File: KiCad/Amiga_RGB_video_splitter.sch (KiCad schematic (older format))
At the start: 5 parts, among them J1 DB23_Female-Connector, J2 DB15_Female_HighDensity_Mount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, J3 KMDGX-9S-BS-1, J4 PJ-320A, U1 THS7374IPWR

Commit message: Add capacitor and route VCC to pin 10 on U1, add resistor R1 to Csync line
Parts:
- added C2: 0.1uF, Capacitor_SMD:C_0805_2012Metric_Pad1.18x1.45mm_HandSolder, symbol Device:C_Small
- added R?: R_Small, Resistor_SMD:R_1206_3216Metric_Pad1.30x1.75mm_HandSolder, symbol Device:R_Small
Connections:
- net +5V: now also U1.10 (VS+), C2.1
- net CSYNC: now also R?.1; no longer J3.4
- net GND: now also C2.2
- new net: J3.4, R?.2
- no-connect marks 12 -> 20
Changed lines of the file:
@@
 GND
 NoConn ~ 1650 3700
-Wire Wire Line
-	4300 2700 4300 3900
 $Comp
 L Amiga_RGB_video_splitter:THS7374IPWR U1
@@
 Wire Wire Line
 	3550 5600 3650 5600
+NoConn ~ 2400 4350
+NoConn ~ 3800 4350
+Text GLabel 4150 4150 2    50   Input ~ 0
+VCC
+$Comp
+L Device:C_Small C2
+U 1 1 6832D346
+P 3950 4250
+F 0 "C2" H 4042 4296 50  0000 L CNN
+F 1 "0.1uF" H 4042 4205 50  0000 L CNN
+F 2 "Capacitor_SMD:C_0805_2012Metric_Pad1.18x1.45mm_HandSolder" H 3950 4250 50  0001 C CNN
+F 3 "~" H 3950 4250 50  0001 C CNN
+	1    3950 4250
+	1    0    0    -1
+$EndComp
+Text GLabel 3950 4350 3    50   Input ~ 0
+GND
+Wire Wire Line
+	3800 4150 3950 4150
+Connection ~ 3950 4150
+Wire Wire Line
+	3950 4150 4150 4150
+NoConn ~ 3450 5600
+NoConn ~ 2850 5000
+NoConn ~ 3050 5000
+NoConn ~ 3650 5000
+NoConn ~ 3350 5600
+$Comp
+L Device:R_Small R?
+U 1 1 68333376
+P 4300 3350
+F 0 "R?" H 4359 3396 50  0000 L CNN
+F 1 "R_Small" H 4359 3305 50  0000 L CNN
+F 2 "Resistor_SMD:R_1206_3216Metric_Pad1.30x1.75mm_HandSolder" H 4300 3350 50  0001 C CNN
+F 3 "~" H 4300 3350 50  0001 C CNN
+	1    4300 3350
+	1    0    0    -1
+$EndComp
+NoConn ~ 4400 2700
+Wire Wire Line
+	4300 2700 4300 3250
+Wire Wire Line
+	4300 3900 4300 3450
 $EndSCHEMATC

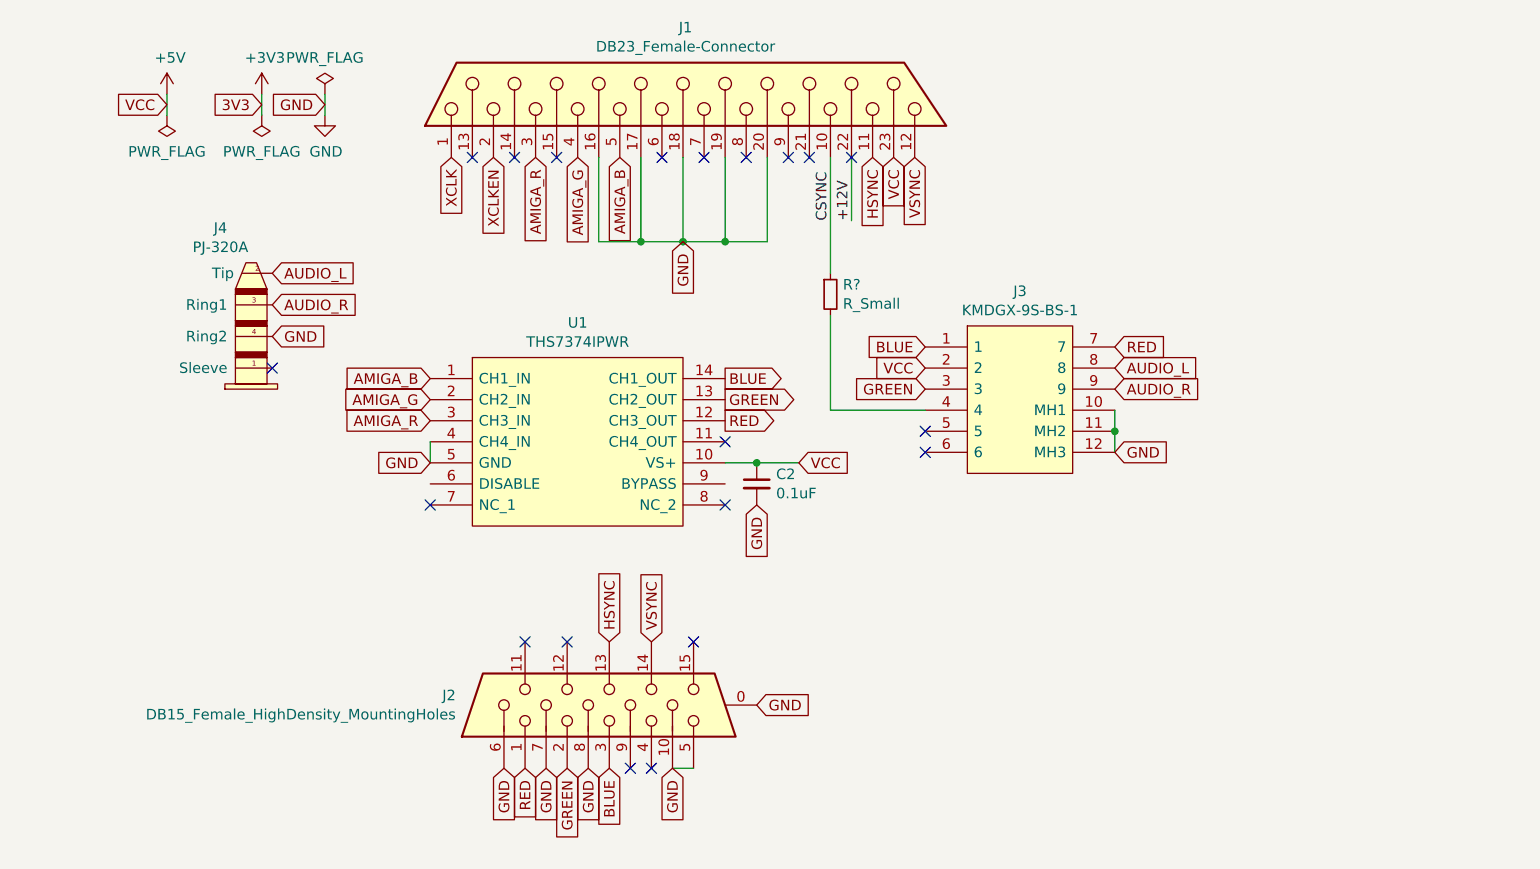
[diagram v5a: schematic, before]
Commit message: Add 75 Ω termination for RGB lines with resistor pack RN1
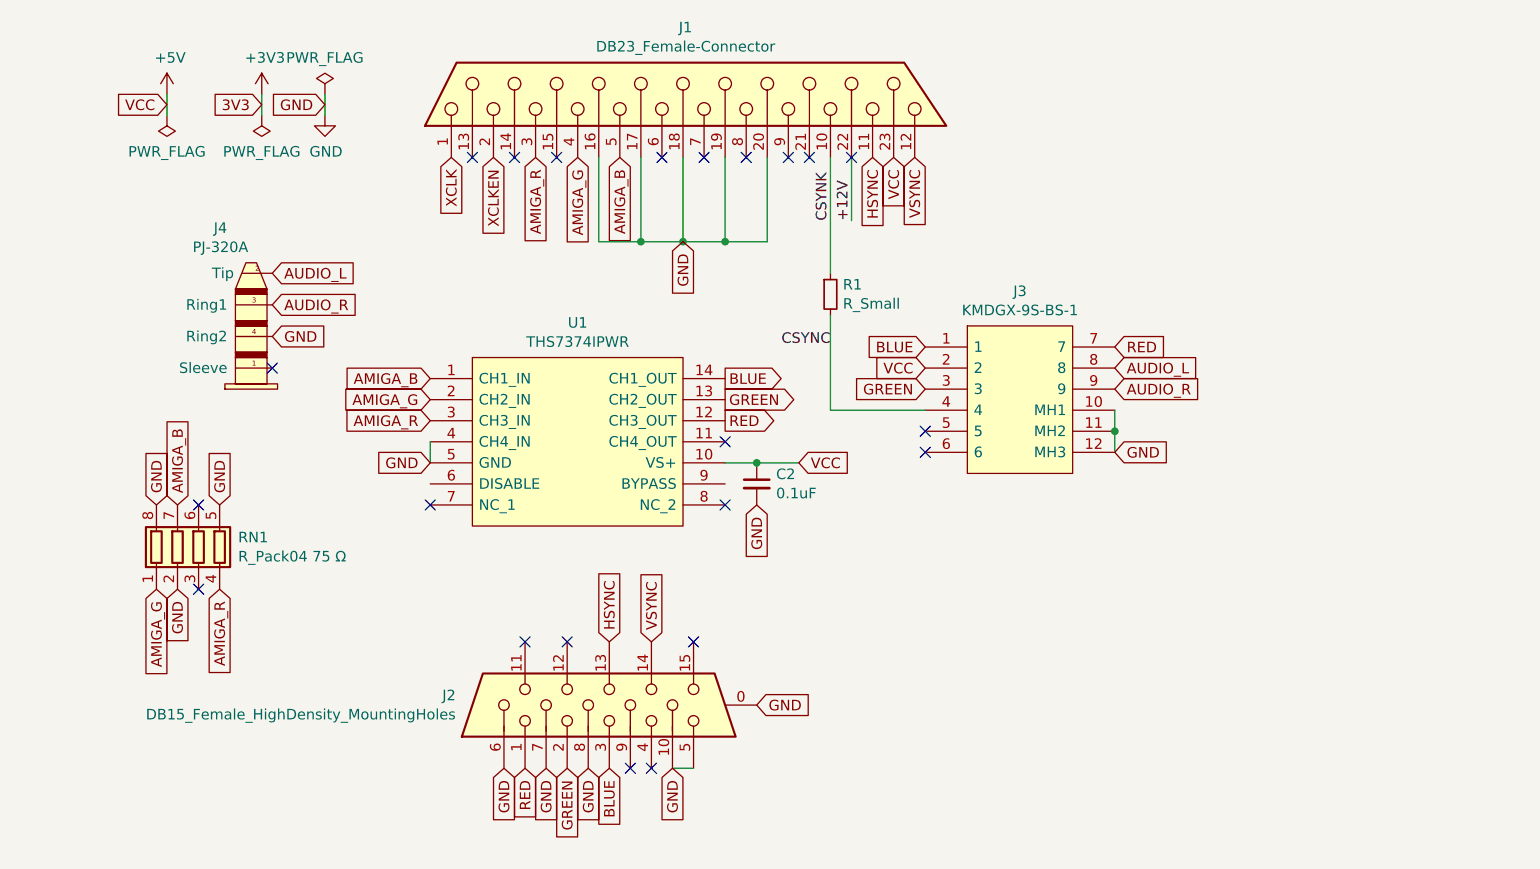
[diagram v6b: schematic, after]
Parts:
- added RN1: R_Pack04 75 Ω, Amiga_RGB_video_splitter:RESCAF80P320X160X60-8N, symbol Device:R_Pack04
- gave numbers to parts that had none: 1
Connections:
- net AMIGA_B: now also RN1.7 (R2.2)
- net AMIGA_G: now also RN1.1 (R1.1)
- net AMIGA_R: now also RN1.4 (R4.1)
- net CSYNC: now also J3.4, R1.2; no longer J1.10, R1.1
- net GND: now also RN1.2 (R2.1), RN1.5 (R4.2), RN1.8 (R1.2)
- new net CSYNK: J1.10, R1.1
- no-connect marks 20 -> 22
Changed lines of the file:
@@
 NoConn ~ 4200 2700
 Text Label 4300 3000 1    50   ~ 0
-CSYNC
+CSYNK
 Wire Wire Line
 	4400 2700 4400 3000
@@
 NoConn ~ 3350 5600
 $Comp
-L Device:R_Small R?
+L Device:R_Small R1
 U 1 1 68333376
 P 4300 3350
-F 0 "R?" H 4359 3396 50  0000 L CNN
+F 0 "R1" H 4359 3396 50  0000 L CNN
 F 1 "R_Small" H 4359 3305 50  0000 L CNN
 F 2 "Resistor_SMD:R_1206_3216Metric_Pad1.30x1.75mm_HandSolder" H 4300 3350 50  0001 C CNN
@@
 Wire Wire Line
 	4300 3900 4300 3450
+$Comp
+L Device:R_Pack04 RN1
+U 1 1 68337CD7
+P 1300 4550
+F 0 "RN1" H 1488 4596 50  0000 L CNN
+F 1 "R_Pack04 75 Ω" H 1488 4505 50  0000 L CNN
+F 2 "Amiga_RGB_video_splitter:RESCAF80P320X160X60-8N" V 1575 4550 50  0001 C CNN
+F 3 "~" H 1300 4550 50  0001 C CNN
+	1    1300 4550
+	1    0    0    -1
+$EndComp
+Text GLabel 1200 4350 1    50   Input ~ 0
+AMIGA_B
+Text GLabel 1100 4750 3    50   Input ~ 0
+AMIGA_G
+Text GLabel 1400 4750 3    50   Input ~ 0
+AMIGA_R
+Text GLabel 1400 4350 1    50   Input ~ 0
+GND
+Text GLabel 1200 4750 3    50   Input ~ 0
+GND
+Text GLabel 1100 4350 1    50   Input ~ 0
+GND
+NoConn ~ 1300 4350
+NoConn ~ 1300 4750
+Text Label 4300 3600 2    50   ~ 0
+CSYNC
 $EndSCHEMATC

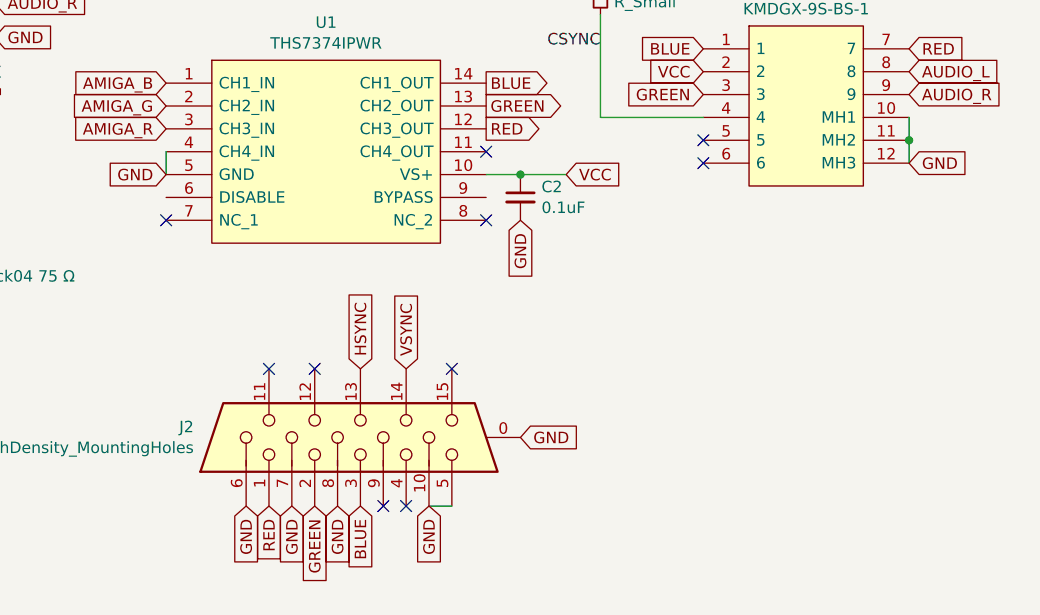
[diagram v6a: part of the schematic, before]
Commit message: Add series resistor for VGA RGB lines with resistor pack RN2
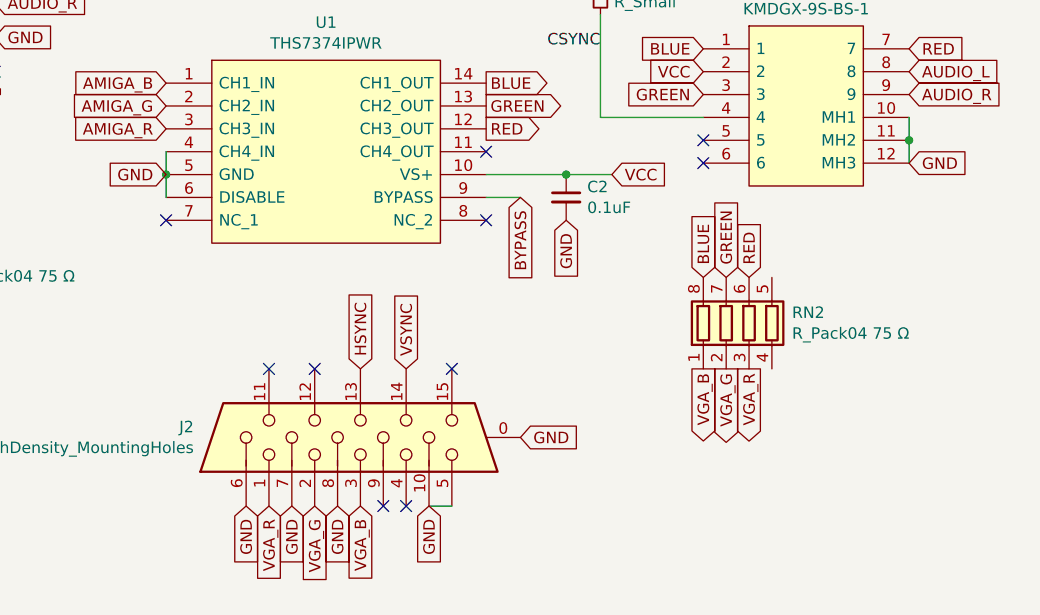
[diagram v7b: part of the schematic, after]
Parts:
- added RN2: R_Pack04 75 Ω, Amiga_RGB_video_splitter:RESCAF80P320X160X60-8N, symbol Device:R_Pack04
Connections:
- net BLUE: now also RN2.8 (R1.2); no longer J2.3
- net GND: now also U1.6 (DISABLE)
- net GREEN: now also RN2.7 (R2.2); no longer J2.2
- net RED: now also RN2.6 (R3.2); no longer J2.1
- net BYPASS: now reaches U1.9 (BYPASS)
- new net VGA_B: J2.3, RN2.1 (R1.1)
- new net VGA_G: J2.2, RN2.2 (R2.1)
- new net VGA_R: J2.1, RN2.3 (R3.1)
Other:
- moved on the sheet: C2
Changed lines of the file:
@@
 AMIGA_B
 Text GLabel 2850 5600 3    50   Input ~ 0
-RED
+VGA_R
 Text GLabel 3050 5600 3    50   Input ~ 0
-GREEN
+VGA_G
 Text GLabel 3250 5600 3    50   Input ~ 0
-BLUE
+VGA_B
 Text GLabel 2750 5600 3    50   Input ~ 0
 GND
@@
 NoConn ~ 2400 4350
 NoConn ~ 3800 4350
-Text GLabel 4150 4150 2    50   Input ~ 0
+Text GLabel 4350 4150 2    50   Input ~ 0
 VCC
 $Comp
 L Device:C_Small C2
 U 1 1 6832D346
-P 3950 4250
-F 0 "C2" H 4042 4296 50  0000 L CNN
-F 1 "0.1uF" H 4042 4205 50  0000 L CNN
-F 2 "Capacitor_SMD:C_0805_2012Metric_Pad1.18x1.45mm_HandSolder" H 3950 4250 50  0001 C CNN
-F 3 "~" H 3950 4250 50  0001 C CNN
-	1    3950 4250
+P 4150 4250
+F 0 "C2" H 4242 4296 50  0000 L CNN
+F 1 "0.1uF" H 4242 4205 50  0000 L CNN
+F 2 "Capacitor_SMD:C_0805_2012Metric_Pad1.18x1.45mm_HandSolder" H 4150 4250 50  0001 C CNN
+F 3 "~" H 4150 4250 50  0001 C CNN
+	1    4150 4250
 	1    0    0    -1
 $EndComp
-Text GLabel 3950 4350 3    50   Input ~ 0
+Text GLabel 4150 4350 3    50   Input ~ 0
 GND
+Connection ~ 4150 4150
 Wire Wire Line
-	3800 4150 3950 4150
-Connection ~ 3950 4150
-Wire Wire Line
-	3950 4150 4150 4150
+	4150 4150 4350 4150
 NoConn ~ 3450 5600
 NoConn ~ 2850 5000
@@
 Text Label 4300 3600 2    50   ~ 0
 CSYNC
+Wire Wire Line
+	2400 4250 2400 4150
+Connection ~ 2400 4150
+Text GLabel 3950 4250 3    50   Input ~ 0
+BYPASS
+Wire Wire Line
+	3800 4150 4150 4150
+Wire Wire Line
+	3800 4250 3950 4250
+$Comp
+L Device:R_Pack04 RN2
+U 1 1 68354B66
+P 4950 4800
+F 0 "RN2" H 5138 4846 50  0000 L CNN
+F 1 "R_Pack04 75 Ω" H 5138 4755 50  0000 L CNN
+F 2 "Amiga_RGB_video_splitter:RESCAF80P320X160X60-8N" V 5225 4800 50  0001 C CNN
+F 3 "~" H 4950 4800 50  0001 C CNN
+	1    4950 4800
+	1    0    0    -1
+$EndComp
+Text GLabel 4750 4600 1    50   Input ~ 0
+BLUE
+Text GLabel 4850 4600 1    50   Input ~ 0
+GREEN
+Text GLabel 4950 4600 1    50   Input ~ 0
+RED
+Text GLabel 4750 5000 3    50   Output ~ 0
+VGA_B
+Text GLabel 4850 5000 3    50   Output ~ 0
+VGA_G
+Text GLabel 4950 5000 3    50   Output ~ 0
+VGA_R
 $EndSCHEMATC

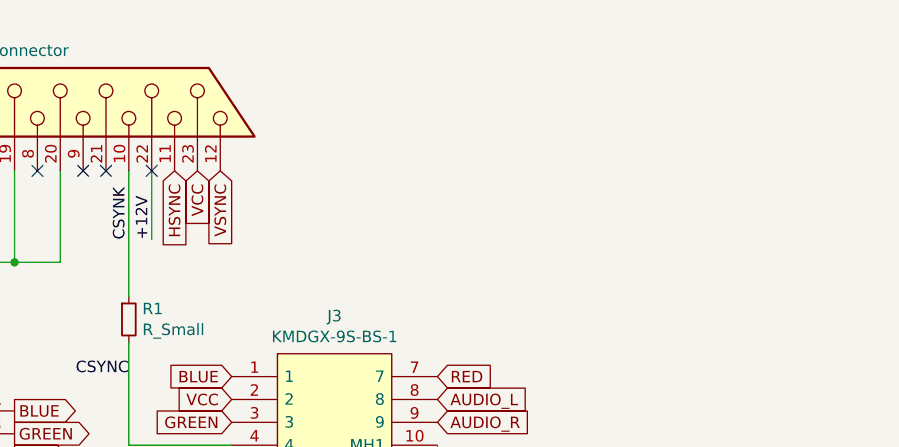
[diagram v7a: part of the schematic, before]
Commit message: Add U2 (74HCT2G17) in TSOP-6 to the design for V-sync and H-sync buffering
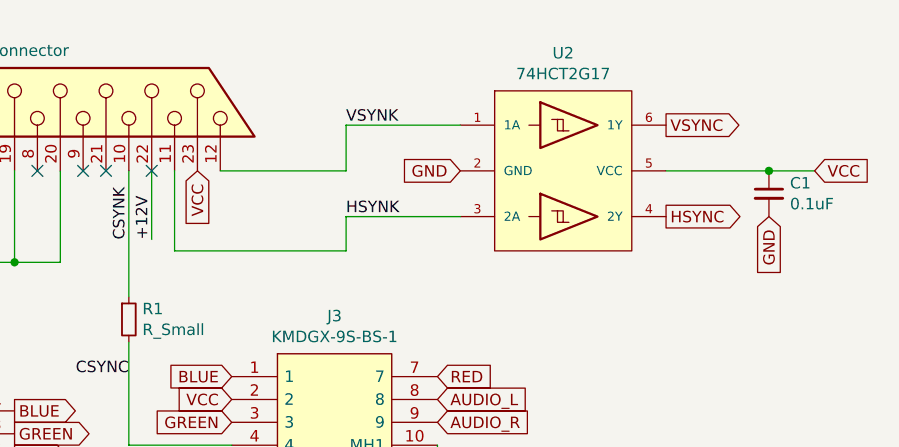
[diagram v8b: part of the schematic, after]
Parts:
- added C1: 0.1uF, Capacitor_SMD:C_0805_2012Metric_Pad1.18x1.45mm_HandSolder, symbol Device:C_Small
- added U2: 74HCT2G17, Package_SO:TSOP-6_1.65x3.05mm_P0.95mm, symbol Amiga_RGB_video_splitter:74HCT2G17
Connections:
- net +5V: now also C1.1, U2.5 (VCC)
- net GND: now also C1.2, U2.2 (GND)
- net HSYNC: now also U2.4 (2Y); no longer J1.11
- net VSYNC: now also U2.6 (1Y); no longer J1.12
- new net HSYNK: J1.11, U2.3 (2A)
- new net VSYNK: J1.12, U2.1 (1A)
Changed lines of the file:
@@
 Text Label 4400 3000 1    50   ~ 0
 +12V
-Text GLabel 4500 2700 3    50   Input ~ 0
+Text GLabel 6650 2900 2    50   Output ~ 0
 HSYNC
-Text GLabel 4700 2700 3    50   Input ~ 0
+Text GLabel 6650 2500 2    50   Output ~ 0
 VSYNC
 Text GLabel 5650 3600 2    50   Input ~ 0
@@
 Text GLabel 4950 5000 3    50   Output ~ 0
 VGA_R
+$Comp
+L Amiga_RGB_video_splitter:74HCT2G17 U2
+U 1 1 68346213
+P 6200 2700
+F 0 "U2" H 6200 3215 50  0000 C CNN
+F 1 "74HCT2G17" H 6200 3124 50  0000 C CNN
+F 2 "Package_SO:TSOP-6_1.65x3.05mm_P0.95mm" H 6700 3650 50  0001 C CNN
+F 3 "https://assets.nexperia.com/documents/data-sheet/74HC_HCT2G17.pdf" H 6700 3650 50  0001 C CNN
+	1    6200 2700
+	1    0    0    -1
+$EndComp
+Text GLabel 5750 2700 0    50   Input ~ 0
+GND
+Text GLabel 7300 2700 2    50   Input ~ 0
+VCC
+$Comp
+L Device:C_Small C1
+U 1 1 68348604
+P 7100 2800
+F 0 "C1" H 7192 2846 50  0000 L CNN
+F 1 "0.1uF" H 7192 2755 50  0000 L CNN
+F 2 "Capacitor_SMD:C_0805_2012Metric_Pad1.18x1.45mm_HandSolder" H 7100 2800 50  0001 C CNN
+F 3 "~" H 7100 2800 50  0001 C CNN
+	1    7100 2800
+	1    0    0    -1
+$EndComp
+Text GLabel 7100 2900 3    50   Input ~ 0
+GND
+Connection ~ 7100 2700
+Wire Wire Line
+	7100 2700 7300 2700
+Wire Wire Line
+	5750 2500 5250 2500
+Wire Wire Line
+	5250 2500 5250 2700
+Wire Wire Line
+	5250 2700 4700 2700
+Text Label 5250 2500 0    50   ~ 0
+VSYNK
+Wire Wire Line
+	6650 2700 7100 2700
+Wire Wire Line
+	4500 2700 4500 3050
+Wire Wire Line
+	4500 3050 5250 3050
+Wire Wire Line
+	5250 3050 5250 2900
+Wire Wire Line
+	5250 2900 5750 2900
+Text Label 5250 2900 0    50   ~ 0
+HSYNK
 $EndSCHEMATC
